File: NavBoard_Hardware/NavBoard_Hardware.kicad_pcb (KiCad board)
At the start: 2 copper layers, 61 x 100.1 mm, 43 parts, among them J1 Conn_Coaxial, U3 OKI, U4 OKI, U5 FGPMMOPA6H

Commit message: generated step file
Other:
- board size 61 x 100.1 mm -> 61 x 100 mm
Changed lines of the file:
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@@
     (47 F.CrtYd user)
     (48 B.Fab user)
-    (49 F.Fab user hide)
+    (49 F.Fab user)
   )
   (setup
-    (last_trace_width 0.762)
+    (last_trace_width 0.25)
     (user_trace_width 0.381)
     (user_trace_width 0.508)
@@
   )
   (module MRDT_Shields:TM4C129E_Launchpad_X9_THT_BOTTOM (layer F.Cu)
-    (at 115.230601 127.024401)
+    (at 115.2652 127.0508)
     (fp_text reference U1 (at 57.404 -0.762 180) (layer F.SilkS) hide
       (effects (font (size 1 1) (thickness 0.15)))
@@
       (xy 1.818986 -2.588809) (xy 1.858404 -2.595946) (xy 1.888683 -2.594105)) (layer F.SilkS) (width 0.01))
   )
+  (gr_line (start 115.2652 137.7188) (end 115.2652 54.483) (layer Edge.Cuts) (width 0.15))
+  (gr_line (start 115.2652 150.4188) (end 115.2652 141.7828) (layer Edge.Cuts) (width 0.15))
+  (gr_line (start 174.1932 152.4508) (end 117.2972 152.4508) (layer Edge.Cuts) (width 0.15))
+  (gr_line (start 176.2252 141.7828) (end 176.2252 150.4188) (layer Edge.Cuts) (width 0.15))
+  (gr_line (start 176.2252 129.5908) (end 176.2252 137.7188) (layer Edge.Cuts) (width 0.15))
+  (gr_line (start 158.4452 127.5588) (end 174.1932 127.5588) (layer Edge.Cuts) (width 0.15))
+  (gr_line (start 158.4452 106.7308) (end 158.4452 127.5588) (layer Edge.Cuts) (width 0.15))
+  (gr_line (start 174.1932 106.7308) (end 158.4452 106.7308) (layer Edge.Cuts) (width 0.15))
+  (gr_line (start 176.2252 54.483) (end 176.2252 104.6988) (layer Edge.Cuts) (width 0.15))
+  (gr_line (start 117.2972 52.451) (end 174.1932 52.451) (layer Edge.Cuts) (width 0.15))
+  (gr_arc (start 117.2972 54.483) (end 117.2972 52.451) (angle -90) (layer Edge.Cuts) (width 0.15))
+  (gr_arc (start 174.1932 54.483) (end 176.2252 54.483) (angle -90) (layer Edge.Cuts) (width 0.15))
+  (gr_arc (start 174.1932 104.6988) (end 174.1932 106.7308) (angle -90) (layer Edge.Cuts) (width 0.15))
+  (gr_arc (start 174.1932 129.5908) (end 176.2252 129.5908) (angle -90) (layer Edge.Cuts) (width 0.15))
+  (gr_arc (start 176.2252 139.7508) (end 176.2252 137.7188) (angle -90) (layer Edge.Cuts) (width 0.15))
+  (gr_arc (start 176.2252 139.7508) (end 174.1932 139.7508) (angle -90) (layer Edge.Cuts) (width 0.15))
+  (gr_arc (start 174.1932 150.4188) (end 174.1932 152.4508) (angle -90) (layer Edge.Cuts) (width 0.15))
+  (gr_arc (start 117.2972 150.4188) (end 115.2652 150.4188) (angle -90) (layer Edge.Cuts) (width 0.15))
+  (gr_arc (start 115.2652 139.7508) (end 115.2652 141.7828) (angle -180) (layer Edge.Cuts) (width 0.15))
   (gr_text "FIX\n" (at 144.526 82.042) (layer F.SilkS)
     (effects (font (size 1.5 1.5) (thickness 0.3)))
@@
   (gr_circle (center 151.13 72.644) (end 152.4 72.898) (layer F.SilkS) (width 0.2))
   (gr_line (start 147.066 71.12) (end 149.352 71.12) (layer F.SilkS) (width 0.2))
-  (gr_arc (start 117.2972 54.478921) (end 117.399059 52.3748) (angle -83.65369847) (layer Edge.Cuts) (width 0.15))
-  (gr_arc (start 174.1805 54.356) (end 176.2125 54.356) (angle -93.93289733) (layer Edge.Cuts) (width 0.15))
   (gr_text "GPS\n\n" (at 143.8965 106.426 90) (layer F.SilkS)
     (effects (font (size 1.5 1.5) (thickness 0.3)))
@@
     (effects (font (size 1.5 1.5) (thickness 0.3)))
   )
-  (gr_line (start 115.2398 150.3934) (end 115.2398 141.7574) (layer Edge.Cuts) (width 0.15))
-  (gr_line (start 117.7544 152.4254) (end 117.2718 152.4254) (layer Edge.Cuts) (width 0.15))
-  (gr_arc (start 117.2718 150.3934) (end 115.2398 150.3934) (angle -90) (layer Edge.Cuts) (width 0.15))
-  (gr_arc (start 115.2144 139.7254) (end 115.2144 141.7574) (angle -180) (layer Edge.Cuts) (width 0.15))
-  (gr_line (start 115.2144 54.1528) (end 115.2144 137.668) (layer Edge.Cuts) (width 0.15))
-  (gr_line (start 174.0535 52.324) (end 117.3988 52.3748) (layer Edge.Cuts) (width 0.15))
-  (gr_line (start 176.1998 104.6734) (end 176.2125 54.356) (layer Edge.Cuts) (width 0.15))
-  (gr_arc (start 174.1678 104.6734) (end 174.142401 106.705399) (angle -90.71615995) (layer Edge.Cuts) (width 0.15))
-  (gr_line (start 158.3944 106.7054) (end 174.1424 106.7054) (layer Edge.Cuts) (width 0.15))
-  (gr_line (start 158.3944 127.508) (end 158.3944 106.7054) (layer Edge.Cuts) (width 0.15))
-  (gr_line (start 174.1678 127.508) (end 158.3944 127.508) (layer Edge.Cuts) (width 0.15))
-  (gr_arc (start 174.1424 129.5654) (end 176.1998 129.5654) (angle -90) (layer Edge.Cuts) (width 0.15))
-  (gr_line (start 176.1998 137.668) (end 176.1998 129.5654) (layer Edge.Cuts) (width 0.15))
-  (gr_arc (start 176.1998 139.7254) (end 176.1998 137.668) (angle -180) (layer Edge.Cuts) (width 0.15))
-  (gr_line (start 176.1998 150.3934) (end 176.1998 141.7828) (layer Edge.Cuts) (width 0.15))
-  (gr_arc (start 174.1678 150.3934) (end 174.1678 152.4254) (angle -90) (layer Edge.Cuts) (width 0.15))
-  (gr_line (start 117.7798 152.4254) (end 174.1678 152.4254) (layer Edge.Cuts) (width 0.15))
   (segment (start 119.8006 123.9744) (end 119.8088 123.9744) (width 0.508) (layer F.Cu) (net 1))
   (segment (start 119.040601 123.214401) (end 119.8006 123.9744) (width 0.508) (layer F.Cu) (net 1))
@@
   (segment (start 117.651102 124.6039) (end 117.651102 121.870898) (width 0.381) (layer B.Cu) (net 7))
   (segment (start 116.500601 125.754401) (end 117.651102 124.6039) (width 0.381) (layer B.Cu) (net 7))
-  (segment (start 143.665 80.25) (end 143.651 80.264) (width 0.381) (layer F.Cu) (net 8))
-  (segment (start 143.665 78.232) (end 143.665 80.25) (width 0.381) (layer F.Cu) (net 8))
-  (segment (start 155.027921 111.633) (end 155.036421 111.6245) (width 0.381) (layer F.Cu) (net 9))
-  (segment (start 154.57 111.633) (end 154.5785 111.6245) (width 0.381) (layer F.Cu) (net 9))
-  (segment (start 152.5185 111.633) (end 154.062 111.633) (width 0.381) (layer F.Cu) (net 9))
-  (segment (start 148.178 77.851) (end 148.209 77.882) (width 0.381) (layer F.Cu) (net 10))
-  (segment (start 145.415 77.851) (end 148.178 77.851) (width 0.381) (layer F.Cu) (net 10))
   (segment (start 169.799 71.363388) (end 167.673606 71.363388) (width 0.381) (layer F.Cu) (net 7))
   (segment (start 156.718 67.76401) (end 144.45299 67.76401) (width 0.381) (layer F.Cu) (net 7))
@@
   (segment (start 165.30001 67.76401) (end 166.116 68.58) (width 0.381) (layer F.Cu) (net 7))
   (segment (start 156.718 67.76401) (end 165.30001 67.76401) (width 0.381) (layer F.Cu) (net 7))
+  (segment (start 143.665 80.25) (end 143.651 80.264) (width 0.381) (layer F.Cu) (net 8))
+  (segment (start 143.665 78.232) (end 143.665 80.25) (width 0.381) (layer F.Cu) (net 8))
+  (segment (start 155.027921 111.633) (end 155.036421 111.6245) (width 0.381) (layer F.Cu) (net 9))
+  (segment (start 154.57 111.633) (end 154.5785 111.6245) (width 0.381) (layer F.Cu) (net 9))
+  (segment (start 152.5185 111.633) (end 154.062 111.633) (width 0.381) (layer F.Cu) (net 9))
+  (segment (start 148.178 77.851) (end 148.209 77.882) (width 0.381) (layer F.Cu) (net 10))
+  (segment (start 145.415 77.851) (end 148.178 77.851) (width 0.381) (layer F.Cu) (net 10))
   (segment (start 116.500601 121.878399) (end 116.500601 123.214401) (width 0.381) (layer F.Cu) (net 11))
   (segment (start 116.459 121.836798) (end 116.500601 121.878399) (width 0.381) (layer F.Cu) (net 11))

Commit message: Finsihed all changes by Andrew Starting PCB
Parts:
- removed Conn3: Molex_SL_08, MRDT_Connectors:MOLEX_SL_08_Horizontal
- added C1: 1uF, Capacitor_SMD:C_0603_1608Metric_Pad1.05x0.95mm_HandSolder, F.Cu at (240.5, 95.4)
- added C2: 22pF, Capacitor_SMD:C_0603_1608Metric_Pad1.05x0.95mm_HandSolder, F.Cu at (236.3, 84.3)
- added C6: 22pF, Capacitor_SMD:C_0603_1608Metric_Pad1.05x0.95mm_HandSolder, F.Cu at (239.7, 84.3)
- added Conn4: External_Connector, MRDT_Connectors:MOLEX_SL_04_Horizontal, F.Cu at (154.7, 65.7)
- added Conn5: Molex_SL_03, MRDT_Connectors:MOLEX_SL_03_Horizontal, F.Cu at (141.7, 65.7)
- added R13: 1K, Resistor_SMD:R_0603_1608Metric_Pad1.05x0.95mm_HandSolder, F.Cu at (236.3, 85.8)
- added R14: 1K, Resistor_SMD:R_0603_1608Metric_Pad1.05x0.95mm_HandSolder, F.Cu at (238.5, 101.1)
- added R15: 1K, Resistor_SMD:R_0603_1608Metric_Pad1.05x0.95mm_HandSolder, F.Cu at (239.7, 85.8)
- added U2: ATMEGA328P, Package_DIP:DIP-28_W7.62mm, F.Cu at (129.3, 86.4)
- added Y1: Crystal, Crystal:Crystal_HC49-U_Vertical, F.Cu at (124.2, 118.5)
- moved Conn1 10.5 mm to (119.6, 110.8)
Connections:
- net TivaRX renamed GPS_RX
- net TivaTX renamed GPS_TX
- R8 pad 1: IMU_SDA -> IMU_RX
- U1 pad PA6: (no net) -> Net-(U1-PadPA6)
- U1 pad PB2: IMU_SCL -> Net-(U1-PadPB2)
- U1 pad PB3: IMU_SDA -> Net-(U1-PadPB3)
- U1 pad PC6: (no net) -> IMU_RX
- U1 pad PC7: (no net) -> IMU_TX
- U1 pad PD0: (no net) -> Net-(U1-PadPD0)
- U1 pad PD1: (no net) -> Net-(U1-PadPD1)
- U1 pad PD3: (no net) -> Net-(U1-PadPD3)
- U1 pad PD7: (no net) -> Net-(U1-PadPD7)
- U1 pad PE3: (no net) -> Net-(U1-PadPE3)
- U1 pad PE4: (no net) -> Net-(U1-PadPE4)
- U1 pad PE5: (no net) -> Net-(U1-PadPE5)
- U1 pad PF3: (no net) -> Net-(U1-PadPF3)
- U1 pad PG0: (no net) -> Net-(U1-PadPG0)
- U1 pad PH2: (no net) -> Net-(U1-PadPH2)
- U1 pad PH3: (no net) -> Net-(U1-PadPH3)
- U1 pad PL4: (no net) -> Net-(U1-PadPL4)
- U1 pad PL5: (no net) -> Net-(U1-PadPL5)
- U1 pad PM3: (no net) -> Net-(U1-PadPM3)
- U1 pad PM4: (no net) -> Net-(U1-PadPM4)
- U1 pad PM5: (no net) -> Net-(U1-PadPM5)
- U1 pad PN2: (no net) -> Net-(U1-PadPN2)
- U1 pad PN3: (no net) -> Net-(U1-PadPN3)
- U1 pad PP2: (no net) -> Net-(U1-PadPP2)
- U1 pad Rese: (no net) -> Net-(U1-PadRese)
- U5 pad 13: (no net) -> Net-(U5-Pad13)
- U5 pad 14: (no net) -> Net-(U5-Pad14)
- U5 pad 15: (no net) -> Net-(U5-Pad15)
- U5 pad 16: (no net) -> Net-(U5-Pad16)
- U5 pad 17: (no net) -> Net-(U5-Pad17)
- U5 pad 18: (no net) -> Net-(U5-Pad18)
- U5 pad 2: (no net) -> Net-(U5-Pad2)
- U5 pad 20: (no net) -> Net-(U5-Pad20)
- U5 pad 6: (no net) -> Net-(U5-Pad6)
- U5 pad 7: (no net) -> Net-(U5-Pad7)
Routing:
- net Net-(U1-PadPB2): track 0.00 -> 78.9 mm
- net IMU_SCL: track 78.9 -> 0.00 mm
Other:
- board text removed: "8 7 6 5 4 3 2 1"
- board text removed: "DRDYM"
- board text removed: "INT1AG"
- board text removed: "INT2AG"
- board text removed: "INTM"

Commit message: Traces and PCB begin
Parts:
- moved R13 94.6 mm to (142.4, 96.9)
- moved R14 91.9 mm to (146.6, 97.0), turned to 180 degrees
- moved C1 85.5 mm to (155.1, 97.0), turned to 180 degrees
- moved C6 80.5 mm to (160.2, 97.0), turned to 180 degrees
- moved R15 79.9 mm to (162.0, 67.2), turned to 180 degrees
- moved C2 73.0 mm to (164.4, 97.0)
- moved C9 47.4 mm to (126.2, 100.7), turned to 90 degrees
- moved Y1 46.0 mm to (167.1, 101.7)
- moved C8 38.1 mm to (126.2, 106.1)
- moved U4 35.4 mm to (127.2, 104.0), turned to 0 degrees
- moved C10 32.2 mm to (138.2, 100.5), turned to 90 degrees
- moved U3 30.3 mm to (137.4, 102.7), turned to 180 degrees
- moved C11 25.5 mm to (138.3, 106.1), turned to 270 degrees
- moved U2 14.1 mm to (140.7, 94.7), turned to 90 degrees
- moved C7 3.15 mm to (172.6, 80.7)
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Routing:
- net +5V: track 117.8 -> 26.4 mm, vias 2 -> 0
- net IMU_SDA: track 87.4 -> 0.00 mm, vias 1 -> 0
- net Net-(U1-PadPB2): track 78.9 -> 0.00 mm
- net GPS_RX: track 69.7 -> 13.6 mm, vias 3 -> 0
- net GPS_TX: track 70.5 -> 22.9 mm, vias 3 -> 1
- net INT1AG: track 39.9 -> 0.00 mm
- net INT2AG: track 39.2 -> 0.00 mm
- net Net-(C10-Pad1): track 58.1 -> 20.5 mm
- net +3V3: track 44.1 -> 9.77 mm
- net Error_LED: track 32.4 -> 0.00 mm
- net DRDYM: track 30.1 -> 0.00 mm
- net SW_Flg1: track 29.3 -> 0.00 mm
- net SW_Flg2: track 28.9 -> 0.00 mm
- net INTM: track 27.0 -> 0.00 mm
- net IMU_RX: track 0.00 -> 22.7 mm
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
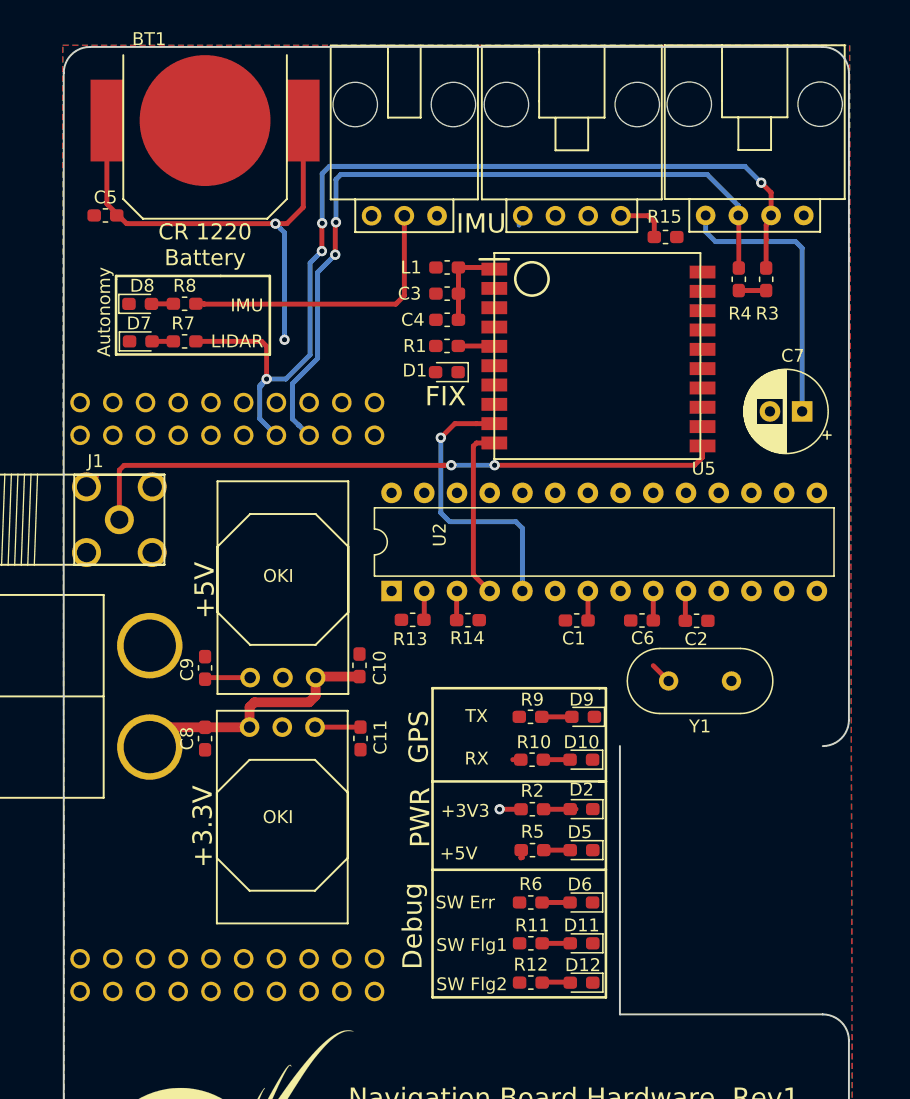
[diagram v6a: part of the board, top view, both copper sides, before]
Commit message: Retracing PCB for Rev 2
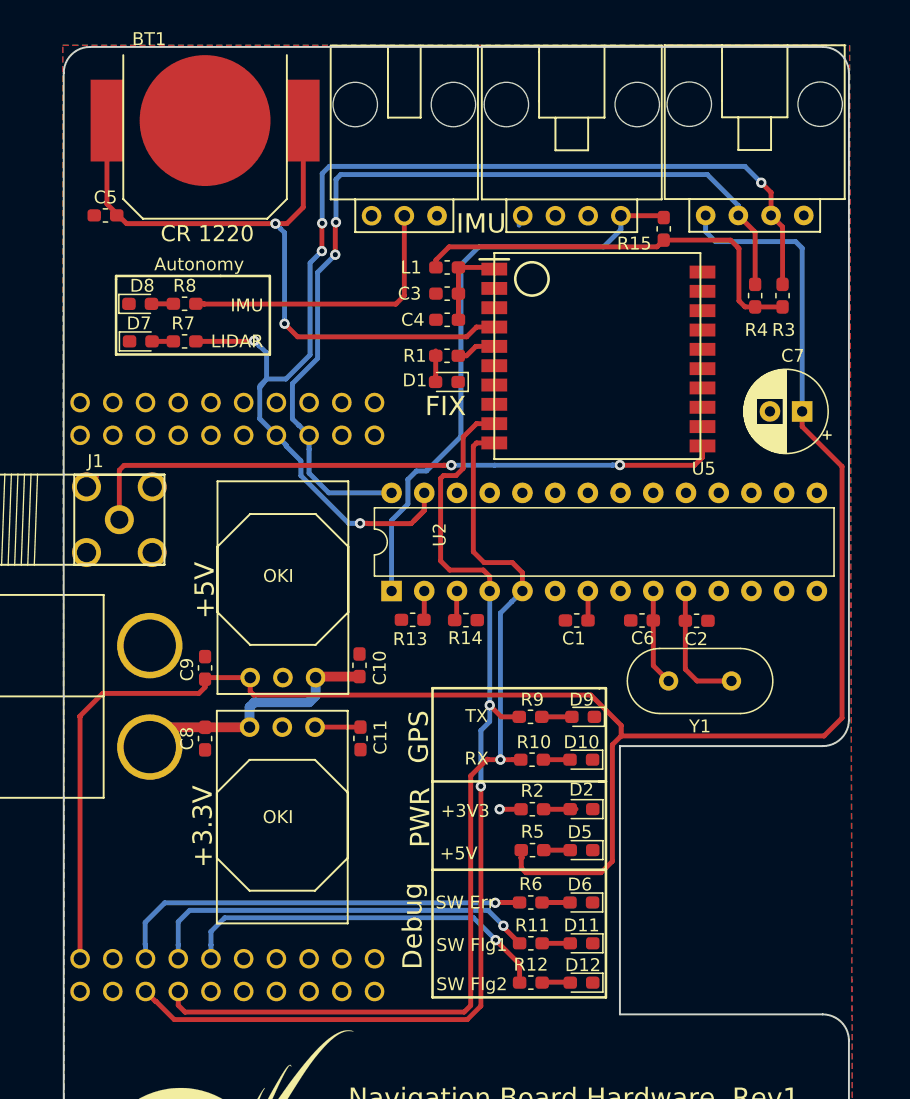
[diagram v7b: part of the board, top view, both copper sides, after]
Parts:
- moved R3 1.80 mm to (171.1, 71.8)
- moved R4 1.80 mm to (168.9, 71.8)
- moved D1 0.76 mm to (145.0, 78.5)
- moved R1 0.76 mm to (145.0, 76.4)
- moved R15 0.65 mm to (161.8, 66.6), turned to 90 degrees
- moved R14 0.15 mm to (146.5, 97.0)
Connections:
- U5 pad 10: GPS_RX -> GPS_TX
- U5 pad 9: GPS_TX -> GPS_RX
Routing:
- net +5V: track 26.4 -> 149.6 mm
- net GPS_RX: track 13.6 -> 81.9 mm, vias 0 -> 2
- net GPS_TX: track 22.9 -> 76.7 mm
- net RESET: track 3.96 -> 46.0 mm
- net Error_LED: track 0.00 -> 32.5 mm, vias 0 -> 1
- net SW_Flg1: track 0.00 -> 30.9 mm, vias 0 -> 1
- net +3V3: track 9.77 -> 40.3 mm
- net SW_Flg2: track 0.00 -> 29.5 mm, vias 0 -> 1
- net LIDAR_SDA: track 75.8 -> 94.6 mm, vias 4 -> 5
- net VBACKUP: track 38.9 -> 54.7 mm
- net LIDAR_SCL: track 59.1 -> 70.9 mm
- net Net-(C2-Pad1): track 2.33 -> 10.1 mm
- net Net-(C6-Pad1): track 3.97 -> 7.48 mm
- net Net-(D1-Pad2): track 0.00 -> 2.04 mm
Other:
- board text added: "3 2 1"
- board text added: "CR 1220"
- board text added: "IMU_RX"
- board text added: "IMU_TX"
- board text added: "PRGM_RX"
- board text added: "PRGM_TX"
- board text added: "RESET"
- board text removed: "CR 1220 Battery"

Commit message: REV2
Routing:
- net IMU_RX: track 22.7 -> 99.4 mm, vias 0 -> 3
- net IMU_TX: track 0.00 -> 69.3 mm, vias 0 -> 4
- net +5V: track 149.6 -> 175.1 mm
- net GPS_RX: track 81.9 -> 62.7 mm
- net GPS_TX: track 76.7 -> 60.9 mm
- net +3V3: track 40.3 -> 28.7 mm
- net GND: track 1.87 -> 7.39 mm
- net RESET: track 46.0 -> 51.3 mm, vias 0 -> 1
- net LIDAR_SCL: track 70.9 -> 72.9 mm, vias 2 -> 1
- net VBACKUP: track 54.7 -> 53.8 mm
- net SW_Flg2: track 29.5 -> 28.7 mm, vias 1 -> 2
- net /EXAnt: track 50.4 -> 49.9 mm, vias 2 -> 0
- net LIDAR_SDA: track 94.6 -> 94.3 mm, vias 5 -> 2
- net SW_Flg1: track 30.9 -> 30.6 mm, vias 1 -> 2
- net Error_LED: track 32.5 -> 32.8 mm, vias 1 -> 2
